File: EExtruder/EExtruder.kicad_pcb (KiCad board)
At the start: 2 copper layers, 64.4 x 47.1 mm, 89 parts, among them J1 20A 50V, J11 Conn_01x03_Male, J2 AudioJack4_Ground, J3 6A 50V, J4 6A 50V, J5 Conn_01x02, J6 Conn_01x02, J7 Conn_01x03_Male, J8 Conn_01x03_Male, J9 Conn_01x03_Male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

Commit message: Added copyright labels.
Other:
- board text added: "(c) iQury.us Oct 2018"
- board text added: "EExtruder rev1"
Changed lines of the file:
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@@
-(kicad_pcb (version 20171130) (host pcbnew 6.0.0-rc1-unknown-6a5744a~66~ubuntu18.04.1)
+(kicad_pcb (version 20171130) (host pcbnew "(5.0.0)")
   (general
     (thickness 1.6)
-    (drawings 38)
+    (drawings 40)
     (tracks 1079)
     (zones 0)
@@
   )
   (setup
-    (last_trace_width 0.508)
+    (last_trace_width 0.1524)
     (user_trace_width 0.1524)
     (user_trace_width 0.3048)
@@
     (zone_45_only no)
     (trace_min 0.127)
+    (segment_width 0.2)
+    (edge_width 0.05)
     (via_size 0.8)
     (via_drill 0.4)
@@
     (uvia_min_size 0.2)
     (uvia_min_drill 0.1)
-    (edge_width 0.05)
-    (segment_width 0.2)
     (pcb_text_width 0.3)
     (pcb_text_size 1.5 1.5)
@@
     (solder_mask_min_width 0.25)
     (aux_axis_origin 127.9525 130.175)
-    (visible_elements FFFFFF7F)
+    (visible_elements 7FFFFFFF)
     (pcbplotparams
       (layerselection 0x010fc_ffffffff)
@@
     )
   )
+  (gr_text "(c) iQury.us\nOct 2018" (at 144.78 111.76) (layer B.SilkS)
+    (effects (font (size 1.5 1.5) (thickness 0.3)) (justify mirror))
+  )
+  (gr_text "EExtruder\nrev1" (at 184.15 92.71) (layer B.SilkS)
+    (effects (font (size 1.5 1.5) (thickness 0.3)) (justify mirror))
+  )
   (gr_text Vin (at 168.9735 91.948) (layer B.SilkS)

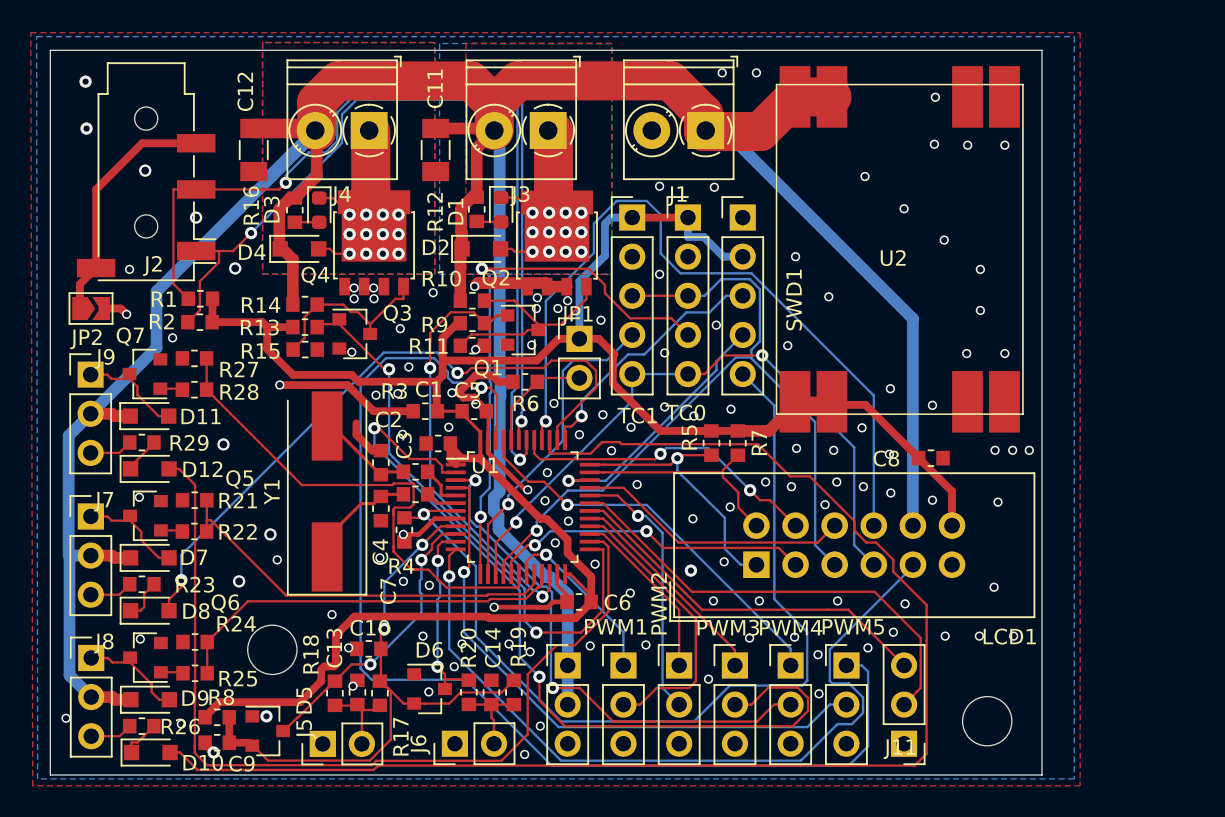
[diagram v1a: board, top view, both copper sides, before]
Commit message: Add fiducials.
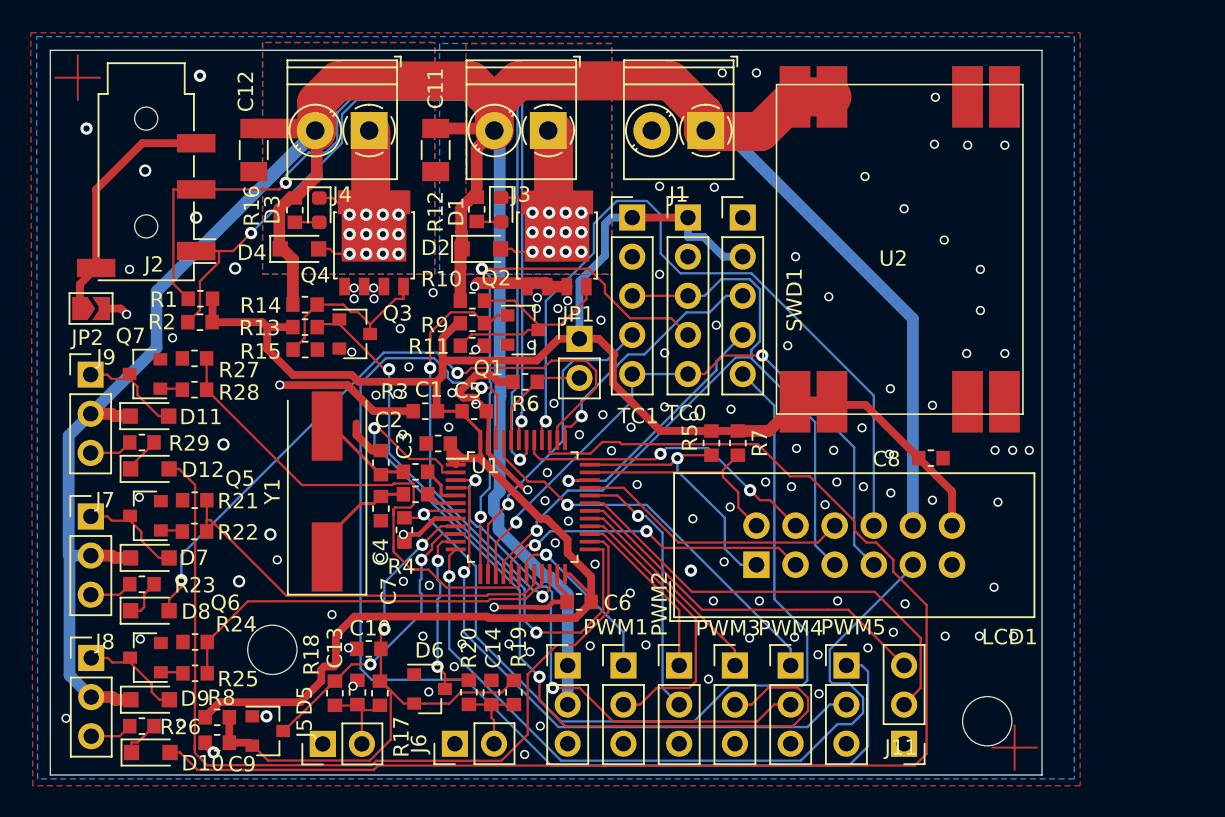
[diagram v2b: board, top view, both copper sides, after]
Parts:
- added FID1: Fiducial, Local:Fiducial_1mm_Dia_2.54mm_Outer_CopperTop, F.Cu at (129.7, 84.9)
- added FID2: Fiducial, Local:Fiducial_1mm_Dia_2.54mm_Outer_CopperTop, F.Cu at (190.6, 128.4)
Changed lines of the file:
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@@
-(kicad_pcb (version 20171130) (host pcbnew "(5.0.0)")
+(kicad_pcb (version 20171130) (host pcbnew 6.0.0-rc1-unknown-6a5744a~66~ubuntu18.04.1)
   (general
     (thickness 1.6)
@@
     (tracks 1079)
     (zones 0)
-    (modules 89)
+    (modules 91)
     (nets 69)
   )
@@
     (zone_45_only no)
     (trace_min 0.127)
-    (segment_width 0.2)
-    (edge_width 0.05)
     (via_size 0.8)
     (via_drill 0.4)
@@
     (uvia_min_size 0.2)
     (uvia_min_drill 0.1)
+    (edge_width 0.05)
+    (segment_width 0.2)
     (pcb_text_width 0.3)
     (pcb_text_size 1.5 1.5)
@@
     (add_net GND)
   )
+  (module Local:Fiducial_1mm_Dia_2.54mm_Outer_CopperTop (layer F.Cu)
+    (at 190.5635 128.397)
+    (descr "Circular Fiducial, 1mm bare copper top; 2.54mm keepout")
+    (tags marker)
+    (attr smd)
+    (fp_text reference FID2 (at -0.3175 -4.2545) (layer F.SilkS) hide
+      (effects (font (size 1 1) (thickness 0.15)))
+    )
+    (fp_text value Fiducial (at 0 -1.8) (layer F.Fab)
+      (effects (font (size 1 1) (thickness 0.15)))
+    )
+    (fp_circle (center 0 0) (end 1.55 0) (layer F.CrtYd) (width 0.05))
+    (pad ~ smd rect (at 0 0) (size 3 0.127) (layers F.Cu F.Paste F.Mask))
+    (pad ~ smd rect (at 0 0) (size 0.127 3) (layers F.Cu F.Paste F.Mask))
+  )
+  (module Local:Fiducial_1mm_Dia_2.54mm_Outer_CopperTop (layer F.Cu)
+    (at 129.7305 84.8995)
+    (descr "Circular Fiducial, 1mm bare copper top; 2.54mm keepout")
+    (tags marker)
+    (attr smd)
+    (fp_text reference FID1 (at 4.2545 0.508) (layer F.SilkS) hide
+      (effects (font (size 1 1) (thickness 0.15)))
+    )
+    (fp_text value Fiducial (at 0 -1.8) (layer F.Fab)
+      (effects (font (size 1 1) (thickness 0.15)))
+    )
+    (fp_circle (center 0 0) (end 1.55 0) (layer F.CrtYd) (width 0.05))
+    (pad ~ smd rect (at 0 0) (size 3 0.127) (layers F.Cu F.Paste F.Mask))
+    (pad ~ smd rect (at 0 0) (size 0.127 3) (layers F.Cu F.Paste F.Mask))
+  )
   (module Jumper:SolderJumper-2_P1.3mm_Open_TrianglePad1.0x1.5mm (layer F.Cu)
     (at 130.593 99.8855)
@@
   (segment (start 131.318 99.8855) (end 132.5245 99.8855) (width 0.508) (layer F.Cu) (net 1))
   (via (at 130.302 88.2015) (size 0.8) (drill 0.4) (layers F.Cu B.Cu) (net 1))
-  (via (at 130.2385 85.1535) (size 0.8) (drill 0.4) (layers F.Cu B.Cu) (net 1))
+  (via (at 137.668 84.7725) (size 0.8) (drill 0.4) (layers F.Cu B.Cu) (net 1))
   (segment (start 153.0345 104.6385) (end 153.0345 106.502) (width 0.508) (layer F.Cu) (net 2))
   (segment (start 153.0345 106.502) (end 153.0855 106.553) (width 0.508) (layer F.Cu) (net 2))

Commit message: Updated EExtruder ground routing. Renamed Nucleo-64 LED values.
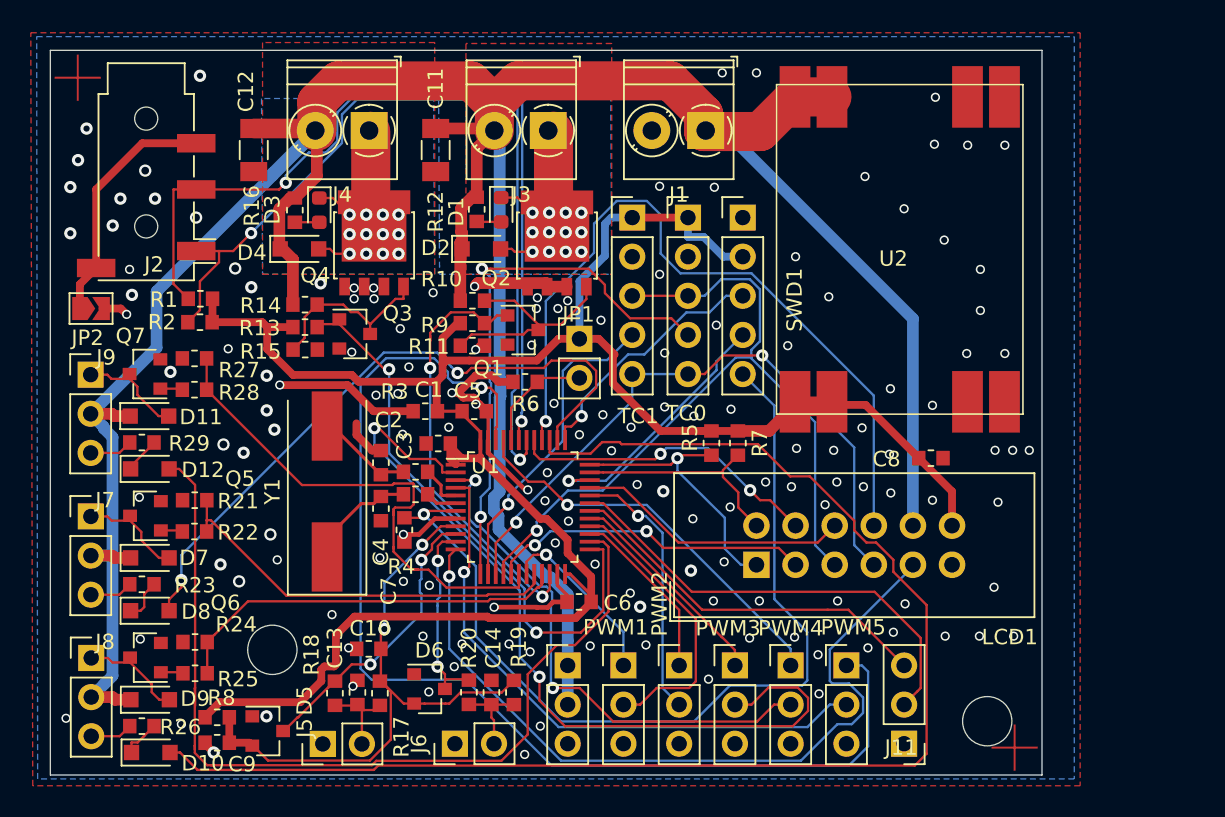
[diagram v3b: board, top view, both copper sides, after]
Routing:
- net GND: vias 133 -> 150
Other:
- board text added: "EExtruder rev2"
- board text removed: "EExtruder rev1"
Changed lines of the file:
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@@
-(kicad_pcb (version 20171130) (host pcbnew 6.0.0-rc1-unknown-6a5744a~66~ubuntu18.04.1)
+(kicad_pcb (version 20171130) (host pcbnew 6.0.0-rc1-unknown-5b3202d~66~ubuntu18.10.1)
   (general
     (thickness 1.6)
     (drawings 40)
-    (tracks 1079)
+    (tracks 1099)
     (zones 0)
     (modules 91)
@@
     (effects (font (size 1.5 1.5) (thickness 0.3)) (justify mirror))
   )
-  (gr_text "EExtruder\nrev1" (at 184.15 92.71) (layer B.SilkS)
+  (gr_text "EExtruder\nrev2" (at 184.15 92.71) (layer B.SilkS)
     (effects (font (size 1.5 1.5) (thickness 0.3)) (justify mirror))
   )
@@
   (via (at 133.7945 121.3485) (size 0.6) (drill 0.4) (layers F.Cu B.Cu) (net 1))
   (via (at 133.731 112.141) (size 0.6) (drill 0.4) (layers F.Cu B.Cu) (net 1))
-  (via (at 135.89 101.7905) (size 0.6) (drill 0.4) (layers F.Cu B.Cu) (net 1))
+  (via (at 139.5 102.5) (size 0.6) (drill 0.4) (layers F.Cu B.Cu) (net 1))
   (via (at 132.9055 100.2665) (size 0.6) (drill 0.4) (layers F.Cu B.Cu) (net 1))
   (via (at 133.096 97.3455) (size 0.6) (drill 0.4) (layers F.Cu B.Cu) (net 1))
@@
   (via (at 130.302 88.2015) (size 0.8) (drill 0.4) (layers F.Cu B.Cu) (net 1))
   (via (at 137.668 84.7725) (size 0.8) (drill 0.4) (layers F.Cu B.Cu) (net 1))
+  (via (at 142 106.5) (size 0.8) (drill 0.4) (layers F.Cu B.Cu) (net 1))
+  (via (at 135.75 104) (size 0.8) (drill 0.4) (layers F.Cu B.Cu) (net 1))
+  (via (at 140.5 109.25) (size 0.8) (drill 0.4) (layers F.Cu B.Cu) (net 1))
+  (via (at 142.5 107.75) (size 0.8) (drill 0.4) (layers F.Cu B.Cu) (net 1))
+  (via (at 142 104.25) (size 0.8) (drill 0.4) (layers F.Cu B.Cu) (net 1))
+  (via (at 141 98.5) (size 0.8) (drill 0.4) (layers F.Cu B.Cu) (net 1))
+  (via (at 145.5 98.25) (size 0.8) (drill 0.4) (layers F.Cu B.Cu) (net 1))
+  (via (at 129.75 90.25) (size 0.8) (drill 0.4) (layers F.Cu B.Cu) (net 1))
+  (via (at 132.5 92.75) (size 0.8) (drill 0.4) (layers F.Cu B.Cu) (net 1))
+  (via (at 132 94.5) (size 0.8) (drill 0.4) (layers F.Cu B.Cu) (net 1))
+  (via (at 134.75 92.75) (size 0.8) (drill 0.4) (layers F.Cu B.Cu) (net 1))
+  (via (at 133.25 99) (size 0.8) (drill 0.4) (layers F.Cu B.Cu) (net 1))
+  (via (at 129.25 95) (size 0.8) (drill 0.4) (layers F.Cu B.Cu) (net 1))
+  (via (at 129.25 92) (size 0.8) (drill 0.4) (layers F.Cu B.Cu) (net 1))
+  (via (at 139 116.5) (size 0.8) (drill 0.4) (layers F.Cu B.Cu) (net 1))
+  (via (at 166.25 119.25) (size 0.8) (drill 0.4) (layers F.Cu B.Cu) (net 1))
+  (via (at 167.75 111.75) (size 0.8) (drill 0.4) (layers F.Cu B.Cu) (net 1))
   (segment (start 153.0345 104.6385) (end 153.0345 106.502) (width 0.508) (layer F.Cu) (net 2))
   (segment (start 153.0345 106.502) (end 153.0855 106.553) (width 0.508) (layer F.Cu) (net 2))
@@
   (segment (start 171.8037 88.392) (end 183.96 100.5483) (width 0.762) (layer B.Cu) (net 7))
   (segment (start 183.96 100.5483) (end 183.96 113.982) (width 0.762) (layer B.Cu) (net 7))
-  (segment (start 130.568 106.721) (end 129.1402 108.1488) (width 0.762) (layer B.Cu) (net 7))
-  (segment (start 129.1402 108.1488) (end 129.1402 115.8719) (width 0.762) (layer B.Cu) (net 7))
-  (segment (start 129.1402 115.8719) (end 129.1963 115.928) (width 0.762) (layer B.Cu) (net 7))
-  (segment (start 129.1963 115.928) (end 129.1963 123.7053) (width 0.762) (layer B.Cu) (net 7))
-  (segment (start 129.1963 123.7053) (end 130.607 125.116) (width 0.762) (layer B.Cu) (net 7))
-  (segment (start 130.58 115.928) (end 129.1963 115.928) (width 0.762) (layer B.Cu) (net 7))
   (segment (start 134.8501 98.7799) (end 134.8501 102.4389) (width 0.762) (layer B.Cu) (net 7))
   (segment (start 134.8501 102.4389) (end 130.568 106.721) (width 0.762) (layer B.Cu) (net 7))
@@
   (segment (start 145.254 88.376) (end 142.3805 91.2495) (width 0.762) (layer B.Cu) (net 7))
   (segment (start 142.3805 91.2495) (end 134.8501 98.7799) (width 0.762) (layer B.Cu) (net 7))
+  (segment (start 131.417999 107.570999) (end 131.417999 107.667999) (width 0.762) (layer B.Cu) (net 7))
+  (segment (start 130.568 106.721) (end 131.417999 107.570999) (width 0.762) (layer B.Cu) (net 7))
+  (segment (start 131.990401 123.732599) (end 131.456999 124.266001) (width 0.762) (layer B.Cu) (net 7))
+  (segment (start 131.456999 124.266001) (end 130.607 125.116) (width 0.762) (layer B.Cu) (net 7))
+  (segment (start 131.417999 107.667999) (end 131.990401 108.240401) (width 0.762) (layer B.Cu) (net 7))
+  (segment (start 131.918401 115.928) (end 130.58 115.928) (width 0.762) (layer B.Cu) (net 7))
+  (segment (start 131.990401 116) (end 131.918401 115.928) (width 0.762) (layer B.Cu) (net 7))
+  (segment (start 131.990401 108.240401) (end 131.990401 116) (width 0.762) (layer B.Cu) (net 7))
+  (segment (start 131.990401 116) (end 131.990401 123.732599) (width 0.762) (layer B.Cu) (net 7))
   (segment (start 147.892 125.6665) (end 146.444 125.6665) (width 0.1524) (layer F.Cu) (net 8))
   (segment (start 146.444 125.6665) (end 146.431 125.6535) (width 0.1524) (layer F.Cu) (net 8))
@@
     (polygon
       (pts
-        (xy 141.732 82.6135) (xy 141.732 97.663) (xy 152.908 97.663) (xy 152.908 82.6135)
+        (xy 141.662 86.25) (xy 141.732 97.663) (xy 152.908 97.663) (xy 152.838 86.25)
       )
     )
@@
     (polygon
       (pts
-        (xy 153.2255 82.677) (xy 153.2255 97.663) (xy 164.4015 97.663) (xy 164.4015 82.677)
+        (xy 153.162 86.25) (xy 153.2255 97.663) (xy 164.4015 97.663) (xy 164.338 86.25)
       )
     )

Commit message: Added 3.3V LDO, updated TC connectors to 6 pins. Re-arranged the layout.
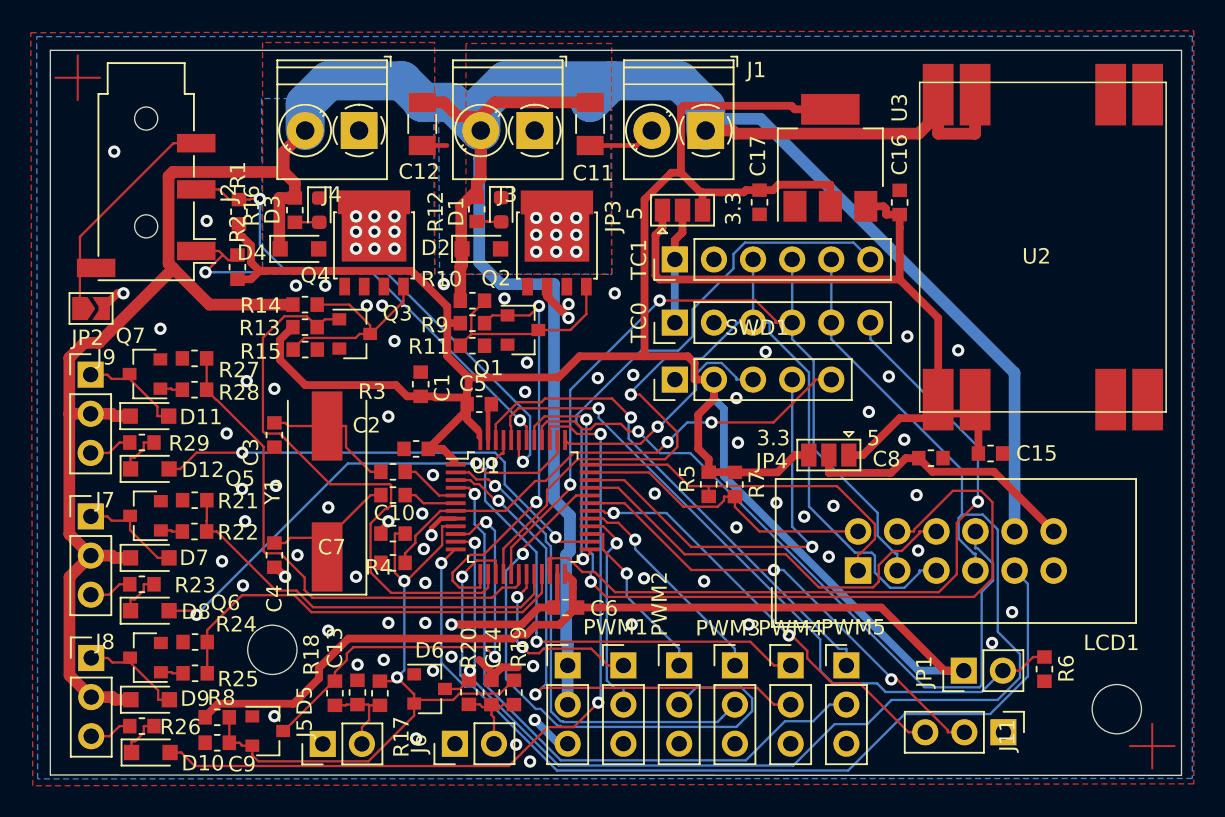
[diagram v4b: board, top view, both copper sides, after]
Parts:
- added C15: 10uF, Local:C_0603_1608Metric, F.Cu at (189.0, 109.3)
- added C16: 10nF, Local:C_0603_1608Metric, F.Cu at (183.1, 93.0)
- added C17: 100nF, Local:C_0603_1608Metric, F.Cu at (174.0, 93.0)
- added JP3: Jumper_3_Open, Jumper:SolderJumper-3_P1.3mm_Open_Pad1.0x1.5mm, F.Cu at (169.0, 93.5)
- added JP4: Jumper_3_Open, Jumper:SolderJumper-3_P1.3mm_Open_Pad1.0x1.5mm, F.Cu at (178.5, 109.4)
- added U3: AMS1117-3.3, Package_TO_SOT_SMD:SOT-223-3_TabPin2, F.Cu at (178.6, 90.1)
- J2: value AudioJack4_Ground -> AudioJack4
- TC0, TC1: value Conn_01x05_Male -> Conn_01x06_Male; footprint Connector_PinHeader_2.54mm:PinHeader_1x05_P2.54mm_Vertical -> Connector_PinHeader_2.54mm:PinHeader_1x06_P2.54mm_Vertical
- moved R6 38.5 mm to (192.5, 123.3), turned to 270 degrees
- moved JP1 33.0 mm to (187.3, 123.4), turned to 90 degrees
- moved SWD1 11.4 mm to (168.5, 104.5), turned to 90 degrees
- moved C12 11.1 mm to (152.1, 87.9)
- moved C11 10.2 mm to (163.0, 87.9)
- moved U2 9.30 mm to (202.4, 85.2)
- moved FID2 8.94 mm to (199.5, 128.3)
- moved H2 8.45 mm to (197.2, 125.9)
- moved C10 7.65 mm to (150.2, 114.5)
- moved C4 7.55 mm to (142.5, 115.9)
- moved C3 7.14 mm to (142.5, 108.1), turned to 270 degrees
- moved TC0 6.87 mm to (168.5, 100.8), turned to 90 degrees
- moved LCD1 6.61 mm to (180.4, 116.9)
- moved J11 6.49 mm to (189.8, 127.4), turned to 270 degrees
- moved R1 6.18 mm to (140.2, 93.6), turned to 90 degrees
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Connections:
- C8 pad 1: /3.3V -> Net-(C8-Pad1)
- LCD1 pad 12: /3.3V -> Net-(C8-Pad1)
- TC0 pad 1: /3.3V -> Net-(JP3-Pad2)
- TC0 pad 4: /~TC0_CS -> /MOSI
- TC1 pad 1: /3.3V -> Net-(JP3-Pad2)
- TC1 pad 4: /~TC1_CS -> /MOSI
- U1 pad 13: /~TC0_CS -> /HEAT0
- U1 pad 14: /~TC1_CS -> /HEAT1
- U1 pad 22: /HEAT0 -> /~TC0_CS
- U1 pad 25: /HEAT1 -> /~TC1_CS
- U2 pad 5: /3.3V -> /5V
- U2 pad 6: /3.3V -> /5V
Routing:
- net /3.3V: track 143.4 -> 206.7 mm
- net /5V: track 0.00 -> 50.1 mm
- net /SPI_CLK: track 42.2 -> 88.4 mm, vias 2 -> 1
- net /PWM5: track 74.7 -> 33.3 mm
- net Net-(JP1-Pad2): track 7.33 -> 46.6 mm, vias 0 -> 1
- net /TACH_E1: track 90.5 -> 51.8 mm, vias 0 -> 2
- net /LCD_LED: track 20.4 -> 55.0 mm
- net /MOSI: track 21.0 -> 54.1 mm
- net /VIN: track 204.9 -> 238.0 mm
- net /TACH0: track 60.3 -> 31.1 mm, vias 0 -> 2
- net /~RESET: track 59.4 -> 33.3 mm, vias 1 -> 2
- net /SCL: track 56.5 -> 30.7 mm
- net /SDA: track 56.3 -> 34.3 mm
- net /TACH3: track 53.7 -> 31.9 mm, vias 2 -> 1
- net /TACH2: track 17.3 -> 38.7 mm
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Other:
- board size 64.4 x 47.1 mm -> 73.4 x 47.1 mm
- net class V5 added: clearance 0.1524, trace_width 0.508, via_dia 0.8, via_drill 0.4
- board text added: "(c) iQury.us Jan 2019"
- board text added: "3.3"
- board text added: "5"
- board text added: "V_PNL"
- board text added: "Vin 12-24V"
- board text removed: "(c) iQury.us Oct 2018"
